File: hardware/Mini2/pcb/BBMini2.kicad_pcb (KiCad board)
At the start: 4 copper layers, 80 x 56 mm, 59 parts, among them J1 Barrel_Jack_Switch, J2 USB_B_Mini, J3 Display, J4 Conn_02x05_Odd_Even, Q1 MBT2222ADW1T1, SW1 SW_SPDT, SW2 SW_Push, SW3 SW_Push, SW4 SW_Push, U1 ESP8266EX, U2 AT25SF081-SSHF-X, U3 AP2112K-3.3, U4 CP2104, U5 MCP3208, Y1 ABM8-26.000MHZ-10-1-U-T

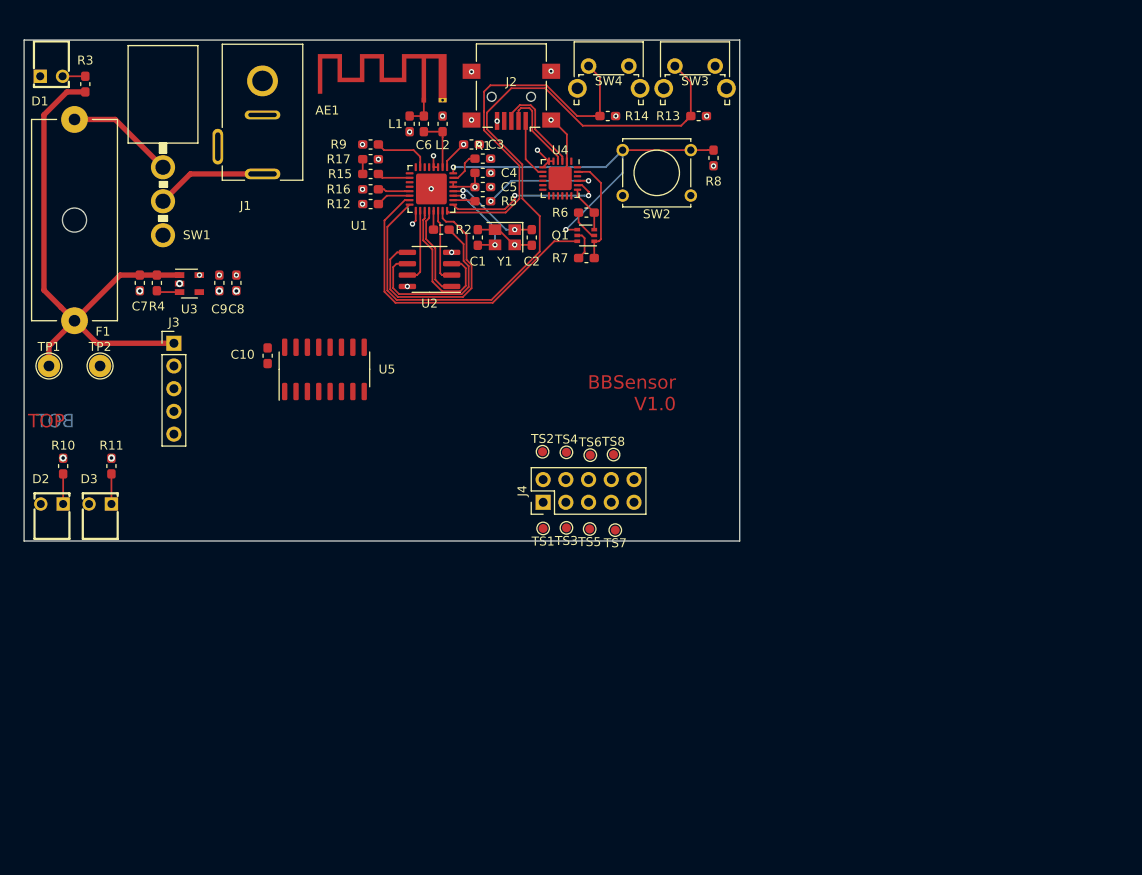
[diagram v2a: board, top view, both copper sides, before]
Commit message: feat: BBMini2 - experimental ESP8266 PCB (SMD)
* add nee stuff

Issue #23
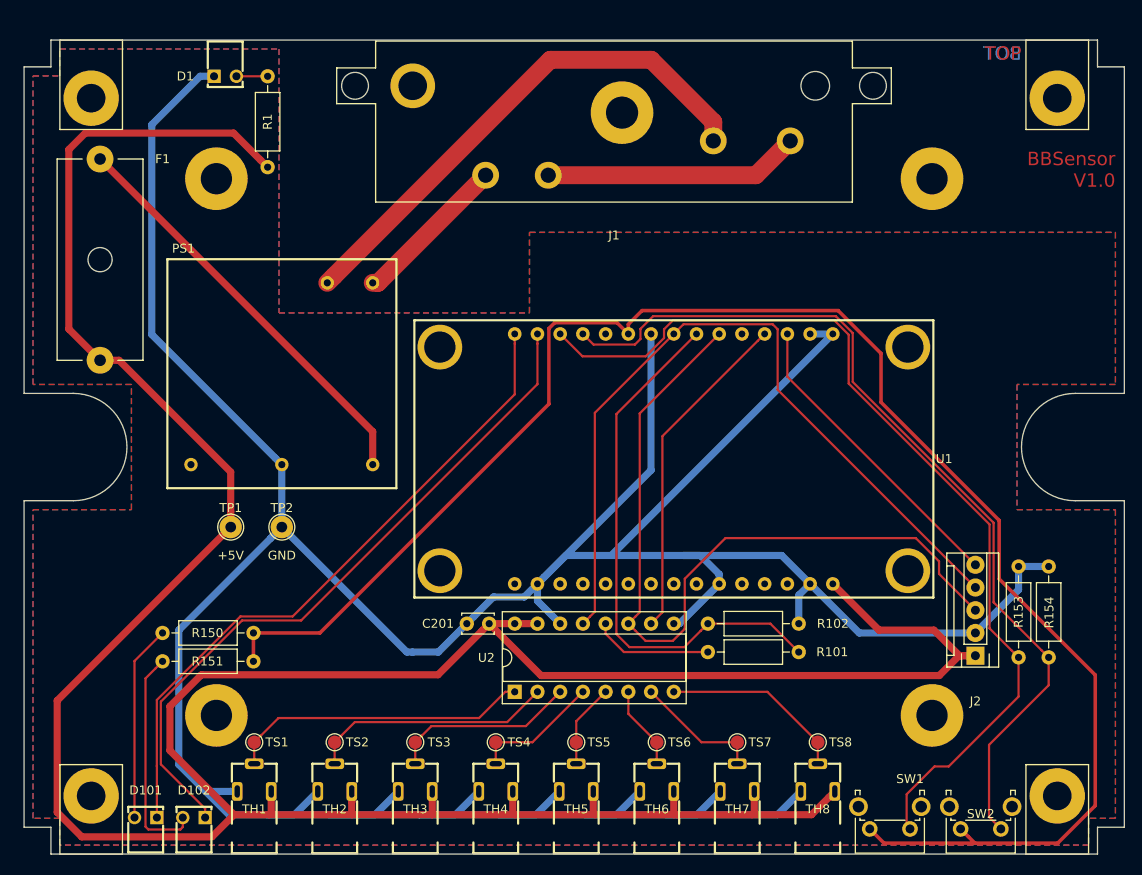
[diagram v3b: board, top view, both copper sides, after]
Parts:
- removed AE1: Antenna_Shield, RF_Antenna:Texas_SWRA117D_2.4GHz_Left
- removed C1, C2: 10p, Capacitor_SMD:C_0603_1608Metric_Pad1.05x0.95mm_HandSolder
- removed C10, C3, C4, C5: 100n, Capacitor_SMD:C_0603_1608Metric_Pad1.05x0.95mm_HandSolder
- removed C6: 5p6, Capacitor_SMD:C_0603_1608Metric_Pad1.05x0.95mm_HandSolder
- removed C7, C8: 10u, Capacitor_SMD:C_0603_1608Metric_Pad1.05x0.95mm_HandSolder
- removed C9: 1u, Capacitor_SMD:C_0603_1608Metric_Pad1.05x0.95mm_HandSolder
- removed D2: LED_RED, VCC:5600F
- removed D3: LED_GREEN, VCC:5600F
- removed J3: Display, Connector_PinHeader_2.54mm:PinHeader_1x05_P2.54mm_Vertical
- removed J4: Conn_02x05_Odd_Even, Connector_PinHeader_2.54mm:PinHeader_2x05_P2.54mm_Vertical
- removed L1, L2: L, Inductor_SMD:L_0603_1608Metric_Pad1.05x0.95mm_HandSolder
- removed Q1: MBT2222ADW1T1, Package_TO_SOT_SMD:SOT-363_SC-70-6
- removed R10, R11: 140, Resistor_SMD:R_0603_1608Metric_Pad1.05x0.95mm_HandSolder
- removed R12, R4, R5, R6, R7, R8, R9: 10k, Resistor_SMD:R_0603_1608Metric_Pad1.05x0.95mm_HandSolder
- removed R13, R14, R17: 2k2, Resistor_SMD:R_0603_1608Metric_Pad1.05x0.95mm_HandSolder
- removed R15: 1k, Resistor_SMD:R_0603_1608Metric_Pad1.05x0.95mm_HandSolder
- removed R16: 4k7, Resistor_SMD:R_0603_1608Metric_Pad1.05x0.95mm_HandSolder
- removed R2: 200, Resistor_SMD:R_0603_1608Metric_Pad1.05x0.95mm_HandSolder
- removed R3: 220, Resistor_SMD:R_0603_1608Metric_Pad1.05x0.95mm_HandSolder
- removed SW3, SW4: SW_Push, Button_Switch_THT:SW_Tactile_SPST_Angled_PTS645Vx83-2LFS
- removed U3: AP2112K-3.3, Package_TO_SOT_SMD:SOT-23-5
- removed U4: CP2104, Package_DFN_QFN:QFN-24-1EP_4x4mm_P0.5mm_EP2.6x2.6mm
- removed U5: MCP3208, Package_SO:SOIC-16_3.9x9.9mm_P1.27mm
- removed Y1: ABM8-26.000MHZ-10-1-U-T, Crystal:Crystal_SMD_Abracon_ABM8G-4Pin_3.2x2.5mm
- added C201: 100n, Capacitor_THT:C_Disc_D3.4mm_W2.1mm_P2.50mm, F.Cu at (67.0, 80.2)
- added D101: RED, VCC:5600F, F.Cu at (28.6, 105.9)
- added D102: GREEN, VCC:5600F, F.Cu at (34.0, 105.9)
- added PS1: TMPS_05, Traco:Traco_TMPS_05, F.Cu at (43.8, 52.3)
- added R101: 1k, Resistor_THT:R_Axial_DIN0207_L6.3mm_D2.5mm_P10.16mm_Horizontal, F.Cu at (91.4, 83.4)
- added R102: 2k2, Resistor_THT:R_Axial_DIN0207_L6.3mm_D2.5mm_P10.16mm_Horizontal, F.Cu at (91.4, 80.2)
- added R150: 140, Resistor_THT:R_Axial_DIN0207_L6.3mm_D2.5mm_P10.16mm_Horizontal, F.Cu at (40.6, 81.3)
- added R151: 140, Resistor_THT:R_Axial_DIN0207_L6.3mm_D2.5mm_P10.16mm_Horizontal, F.Cu at (40.6, 84.5)
- added R153: 2k2, Resistor_THT:R_Axial_DIN0207_L6.3mm_D2.5mm_P10.16mm_Horizontal, F.Cu at (126.2, 84.0)
- added R154: 2k2, Resistor_THT:R_Axial_DIN0207_L6.3mm_D2.5mm_P10.16mm_Horizontal, F.Cu at (129.5, 84.0)
- added TH1: AudioJack3, Lumberg:LUMBERG_1501_05, F.Cu at (40.7, 105.9)
- added TH2: AudioJack3, Lumberg:LUMBERG_1501_05, F.Cu at (49.7, 105.9)
- added TH3: AudioJack3, Lumberg:LUMBERG_1501_05, F.Cu at (58.7, 105.9)
- added TH4: AudioJack3, Lumberg:LUMBERG_1501_05, F.Cu at (67.7, 105.9)
- added TH5: AudioJack3, Lumberg:LUMBERG_1501_05, F.Cu at (76.7, 105.9)
- added TH6: AudioJack3, Lumberg:LUMBERG_1501_05, F.Cu at (85.7, 105.9)
- added TH7: AudioJack3, Lumberg:LUMBERG_1501_05, F.Cu at (94.7, 105.9)
- added TH8: AudioJack3, Lumberg:LUMBERG_1501_05, F.Cu at (103.7, 105.9)
- added ~: Mounting_Bracket_L10_W7_M3, Collection:Mounting_Bracket_L10_W7_M3, F.Cu at (134.0, 15.0)
- added ~: Mounting_Bracket_L10_W7_M3, Collection:Mounting_Bracket_L10_W7_M3, F.Cu at (26.0, 15.0)
- added ~: Mounting_Bracket_L10_W7_M3, Collection:Mounting_Bracket_L10_W7_M3, F.Cu at (127.0, 106.0)
- added ~: Mounting_Bracket_L10_W7_M3, Collection:Mounting_Bracket_L10_W7_M3, F.Cu at (19.0, 106.0)
- added ~: ~, MountingHole:MountingHole_3.5mm_Pad, F.Cu at (36.5, 30.5)
- added ~: ~, MountingHole:MountingHole_3.5mm_Pad, F.Cu at (36.5, 90.5)
- added ~: ~, MountingHole:MountingHole_3.5mm_Pad, F.Cu at (116.5, 30.5)
- added ~: ~, MountingHole:MountingHole_3.5mm_Pad, F.Cu at (116.5, 90.5)
- J1: value Barrel_Jack_Switch -> Schurter_CMF1; footprint Collection:CLIFF_DC_SOCKET_2.5 -> Schurter:CMF1_Offset
- J2: value USB_B_Mini -> Display; footprint Connector_USB:USB_Mini-B_Lumberg_2486_01_Horizontal -> Molex:Molex_KK256_Pin_Header_Straight_1x05
- R1: value 12k -> 220; footprint Resistor_SMD:R_0603_1608Metric_Pad1.05x0.95mm_HandSolder -> Resistor_THT:R_Axial_DIN0207_L6.3mm_D2.5mm_P10.16mm_Horizontal
- SW1: value SW_SPDT -> SW_Push; footprint Collection:MIYAMA_MS-500-B-VT -> Button_Switch_THT:SW_Tactile_SPST_Angled_PTS645Vx83-2LFS
- SW2: footprint Button_Switch_THT:SW_Tactile_Straight_KSL0Axx1LFTR -> Button_Switch_THT:SW_Tactile_SPST_Angled_PTS645Vx83-2LFS
- TS1, TS2, TS3, TS4, TS5, TS6, TS7, TS8: footprint TestPoint:TestPoint_Pad_D1.0mm -> TestPoint:TestPoint_Pad_D1.5mm
- U1: value ESP8266EX -> ESP8266-12E_NodeMCU_Lolin; footprint Package_DFN_QFN:QFN-32-1EP_5x5mm_P0.5mm_EP3.45x3.45mm -> Collection:ESP8266-12E_NodeMCU_Lolin
- U2: value AT25SF081-SSHF-X -> MCP3208; footprint Package_SO:SOIC-8_3.9x4.9mm_P1.27mm -> Package_DIP:DIP-16_W7.62mm_Socket
- moved SW1 110.5 mm to (114.0, 103.2), turned to 180 degrees
- moved J2 81.2 mm to (121.3, 83.8)
- moved SW2 78.8 mm to (124.2, 103.2)
- moved U2 48.2 mm to (69.8, 87.9), turned to 90 degrees
- moved J1 42.0 mm to (80.9, 15.1), turned to 0 degrees
- moved TS1 40.2 mm to (40.7, 93.5)
- moved TS2 39.9 mm to (49.7, 93.5), turned to 180 degrees
- moved TS8 39.4 mm to (103.7, 93.5), turned to 180 degrees
- moved TS4 33.4 mm to (67.7, 93.5), turned to 180 degrees
- moved TS6 32.9 mm to (85.7, 93.5), turned to 180 degrees
- moved U1 31.6 mm to (69.8, 61.8), turned to 90 degrees
- moved TS3 29.3 mm to (58.7, 93.5)
- moved TS7 27.4 mm to (94.7, 93.5)
- moved TP1 27.2 mm to (38.1, 69.4)
- moved TP2 27.2 mm to (43.8, 69.4)
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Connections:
- net /ESP8266EX/ADC renamed Net-(U1-Pad6)
- J1 pad 2: GND -> Net-(J1-Pad2)
- J2 pad 1: Net-(J2-Pad1) -> +5V
- J2 pad 2: Net-(J2-Pad2) -> GND
- J2 pad 3: Net-(J2-Pad3) -> /Analog/Digital/SPI1
- J2 pad 4: Net-(J2-Pad4) -> /Analog/Digital/SPI3
- J2 pad 5: GND -> /Display/SPI5
- R1 pad 1: Net-(R1-Pad1) -> Net-(D1-Pad2)
- R1 pad 2: GND -> +5V
- SW1 pad 1: Net-(SW1-Pad1) -> Net-(R153-Pad1)
- SW1 pad 2: Net-(J1-Pad1) -> +3V3
- SW2 pad 1: GND -> Net-(R154-Pad1)
- SW2 pad 2: /ESP8266EX/~RST -> +3V3
- TS1 pad 1: /Temperature/SIGNAL1 -> /Analog/Digital/SIGNAL1
- TS2 pad 1: /Temperature/SIGNAL2 -> /Analog/Digital/SIGNAL2
- TS3 pad 1: /Temperature/SIGNAL3 -> /Analog/Digital/SIGNAL3
- TS4 pad 1: /Temperature/SIGNAL4 -> /Analog/Digital/SIGNAL4
- TS5 pad 1: /Temperature/SIGNAL5 -> /Analog/Digital/SIGNAL5
- TS6 pad 1: /Temperature/SIGNAL6 -> /Analog/Digital/SIGNAL6
- TS7 pad 1: /Temperature/SIGNAL7 -> /Analog/Digital/SIGNAL7
- TS8 pad 1: /Temperature/SIGNAL8 -> /Analog/Digital/SIGNAL8
- U1 pad 1: +3V3 -> Net-(U1-Pad1)
- U1 pad 10: /ESP8266EX/GPIO12 -> GND
- U1 pad 11: +3V3 -> Net-(U1-Pad11)
- U1 pad 12: /ESP8266EX/GPIO13 -> Net-(U1-Pad12)
- U1 pad 13: /ESP8266EX/GPIO15 -> Net-(U1-Pad13)
- U1 pad 14: /ESP8266EX/GPIO2 -> GND
- U1 pad 15: /ESP8266EX/GPIO0 -> +5V
- U1 pad 16: /ESP8266EX/GPIO4 -> Net-(D101-Pad1)
- U1 pad 17: +3V3 -> Net-(D102-Pad1)
- U1 pad 18: /ESP8266EX/SDIO_DATA_2 -> Net-(R153-Pad1)
- U1 pad 19: /ESP8266EX/SDIO_DATA_3 -> Net-(R154-Pad1)
- U1 pad 2: /ESP8266EX/LNA -> GND
- U1 pad 20: /ESP8266EX/SDIO_CMD -> Net-(U1-Pad20)
- U1 pad 21: /ESP8266EX/SDIO_CLK -> +3V3
- U1 pad 22: /ESP8266EX/SDIO_DATA_0 -> GND
- U1 pad 23: /ESP8266EX/SDIO_DATA_1 -> /Analog/Digital/SPI3
- U1 pad 24: /ESP8266EX/GPIO5 -> /ESP8266/MISO
- U1 pad 25: /ESP8266EX/GPIO1_TXD -> /Analog/Digital/SPI1
- U1 pad 26: /ESP8266EX/GPIO3_RXD -> Net-(U1-Pad26)
- U1 pad 27: /ESP8266EX/XTAL_OUT -> /Analog/Digital/SPI4
- U1 pad 28: /ESP8266EX/XTAL_IN -> /Display/SPI5
- U1 pad 29: +3V3 -> GND
- U1 pad 3: +3V3 -> Net-(U1-Pad3)
- U1 pad 30: +3V3 -> GND
- U1 pad 4: +3V3 -> Net-(U1-Pad4)
- U1 pad 7: /ESP8266EX/EN -> Net-(U1-Pad7)
- U1 pad 8: /IO/CS1 -> Net-(U1-Pad8)
- U1 pad 9: /ESP8266EX/GPIO14 -> Net-(U1-Pad9)
- U2 pad 1: /ESP8266EX/SDIO_CMD -> /Analog/Digital/SIGNAL1
- U2 pad 2: /ESP8266EX/SDIO_DATA_0 -> /Analog/Digital/SIGNAL2
- U2 pad 3: /ESP8266EX/SDIO_DATA_3 -> /Analog/Digital/SIGNAL3
- U2 pad 4: GND -> /Analog/Digital/SIGNAL4
- U2 pad 5: /ESP8266EX/SDIO_DATA_1 -> /Analog/Digital/SIGNAL5
- U2 pad 6: Net-(R2-Pad1) -> /Analog/Digital/SIGNAL6
- U2 pad 7: /ESP8266EX/SDIO_DATA_2 -> /Analog/Digital/SIGNAL7
- U2 pad 8: +3V3 -> /Analog/Digital/SIGNAL8
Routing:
- net GND: track 14.4 -> 411.9 mm, vias 22 -> 0
- net +5V: track 62.4 -> 361.1 mm
- net +3V3: track 14.5 -> 187.2 mm, vias 14 -> 0
- net Net-(R153-Pad1): track 0.00 -> 105.6 mm
- net Net-(R154-Pad1): track 0.00 -> 101.2 mm
- net /Analog/Digital/SPI1: track 0.00 -> 88.4 mm
- net /Analog/Digital/SPI3: track 0.00 -> 86.9 mm
- net /ESP8266EX/GPIO4: track 80.8 -> 0.00 mm
- net Net-(D102-Pad1): track 0.00 -> 77.4 mm
- net Net-(D101-Pad1): track 0.00 -> 74.1 mm
- net /ESP8266/MISO: track 0.00 -> 60.7 mm
- net Net-(J1-Pad1): track 12.4 -> 58.5 mm
- net /ESP8266EX/~RST: track 43.4 -> 0.00 mm, vias 2 -> 0
- net /ESP8266EX/GPIO5: track 43.2 -> 0.00 mm
- net /Analog/Digital/SPI4: track 0.00 -> 37.6 mm
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- added copper zone on F.Cu, net +5V
- added copper zone on B.Cu, net GND
- removed copper zone on In1.Cu, net +3V3
- removed copper zone on In2.Cu, net GND
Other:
- board size 80 x 56 mm -> 123 x 91 mm
- copper layers 4 -> 2
- net class 3V3: clearance 0.125 -> 0.3; trace_width 0.2 -> 0.4; via_dia 0.6 -> 0.8; via_drill 0.3 -> 0.4
- net class 5V: clearance 0.2 -> 0.3; trace_width 0.6 -> 0.8
- net class AC added: clearance 0.4, trace_width 2, via_dia 0.8, via_drill 0.4
- net class Default: clearance 0.125 -> 0.2; trace_width 0.2 -> 0.25; via_dia 0.6 -> 0.8; via_drill 0.3 -> 0.4
- rule trace_clearance: 0.125 -> 0.2
- board text added: "+5V"
- board text added: "GND"

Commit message: feat: BBMini2 - experimental ESP8266 PCB (SMD)
* add reference_

Issue #23
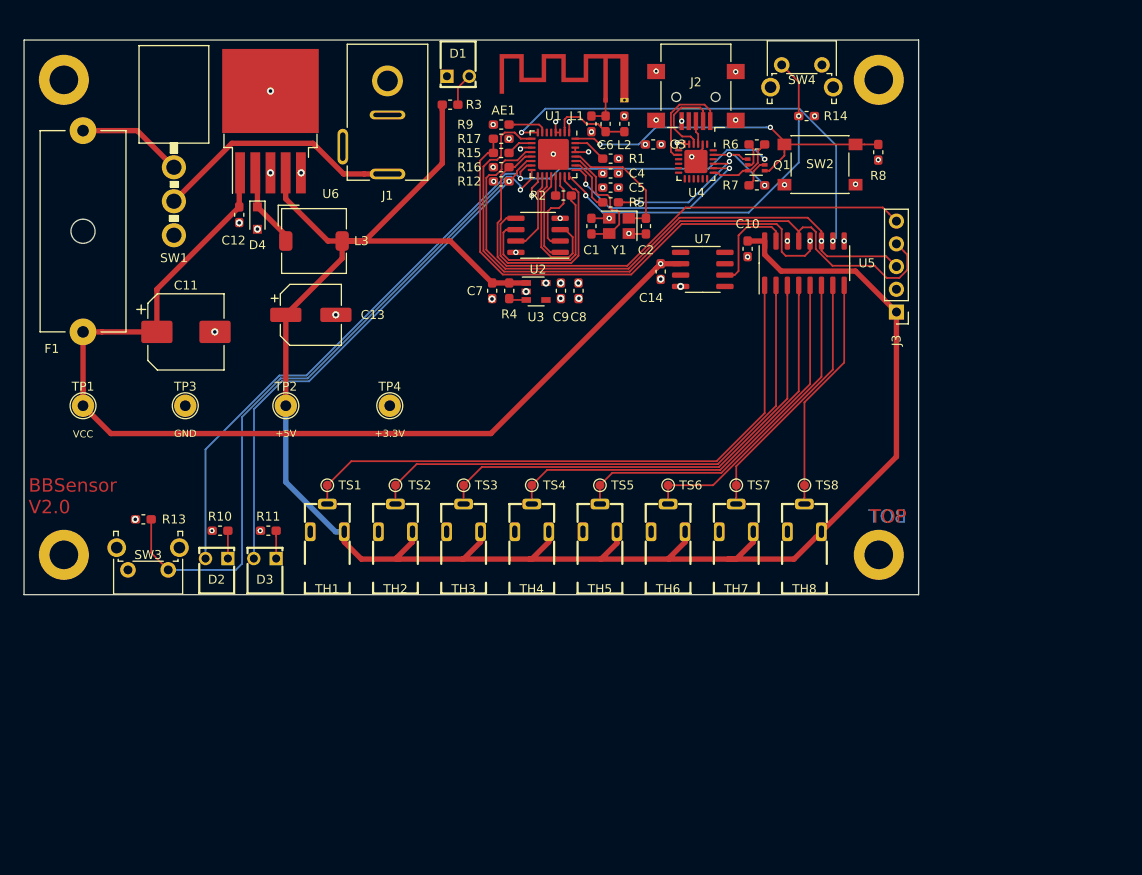
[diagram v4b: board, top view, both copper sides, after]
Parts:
- removed C201: 100n, Capacitor_THT:C_Disc_D3.4mm_W2.1mm_P2.50mm
- removed D101: RED, VCC:5600F
- removed D102: GREEN, VCC:5600F
- removed PS1: TMPS_05, Traco:Traco_TMPS_05
- removed R101: 1k, Resistor_THT:R_Axial_DIN0207_L6.3mm_D2.5mm_P10.16mm_Horizontal
- removed R102, R153, R154: 2k2, Resistor_THT:R_Axial_DIN0207_L6.3mm_D2.5mm_P10.16mm_Horizontal
- removed R150, R151: 140, Resistor_THT:R_Axial_DIN0207_L6.3mm_D2.5mm_P10.16mm_Horizontal
- removed the ~ at (134.0, 15.0)
- removed the ~ at (26.0, 15.0)
- removed the ~ at (127.0, 106.0)
- removed the ~ at (19.0, 106.0)
- removed the ~ at (36.5, 30.5)
- removed the ~ at (36.5, 90.5)
- removed the ~ at (116.5, 30.5)
- removed the ~ at (116.5, 90.5)
- added AE1: Antenna_Shield, RF_Antenna:Texas_SWRA117D_2.4GHz_Left, F.Cu at (80.0, 21.7)
- added C1: 10p, Capacitor_SMD:C_0603_1608Metric_Pad1.05x0.95mm_HandSolder, F.Cu at (78.4, 35.8)
- added C10: 100n, Capacitor_SMD:C_0603_1608Metric_Pad1.05x0.95mm_HandSolder, F.Cu at (95.9, 38.3)
- added C11: 100u, Capacitor_SMD:CP_Elec_8x10, F.Cu at (33.1, 47.6)
- added C12: 100n, Capacitor_SMD:C_0603_1608Metric_Pad1.05x0.95mm_HandSolder, F.Cu at (39.1, 34.5)
- added C13: 100u, Capacitor_SMD:CP_Elec_6.3x5.9, F.Cu at (47.1, 45.7)
- added C14: 100n, Capacitor_SMD:C_0603_1608Metric_Pad1.05x0.95mm_HandSolder, F.Cu at (86.2, 40.9)
- added C2: 10p, Capacitor_SMD:C_0603_1608Metric_Pad1.05x0.95mm_HandSolder, F.Cu at (84.5, 35.8)
- added C3: 100n, Capacitor_SMD:C_0603_1608Metric_Pad1.05x0.95mm_HandSolder, F.Cu at (85.3, 26.7)
- added C4: 100n, Capacitor_SMD:C_0603_1608Metric_Pad1.05x0.95mm_HandSolder, F.Cu at (80.6, 29.9)
- added C5: 100n, Capacitor_SMD:C_0603_1608Metric_Pad1.05x0.95mm_HandSolder, F.Cu at (80.6, 31.5)
- added C6: 5p6, Capacitor_SMD:C_0603_1608Metric_Pad1.05x0.95mm_HandSolder, F.Cu at (80.0, 24.4)
- added C7: 10u, Capacitor_SMD:C_0603_1608Metric_Pad1.05x0.95mm_HandSolder, F.Cu at (67.3, 43.0)
- added C8: 10u, Capacitor_SMD:C_0603_1608Metric_Pad1.05x0.95mm_HandSolder, F.Cu at (77.0, 43.0)
- added C9: 1u, Capacitor_SMD:C_0603_1608Metric_Pad1.05x0.95mm_HandSolder, F.Cu at (75.0, 43.0)
- added D2: LED_RED, VCC:5600F, F.Cu at (36.5, 77.0)
- added D3: LED_GREEN, VCC:5600F, F.Cu at (41.9, 77.0)
- added D4: 1N5822, Diode_SMD:D_SOD-323_HandSoldering, F.Cu at (41.1, 34.9)
- added J3: Display, Connector_PinHeader_2.54mm:PinHeader_1x05_P2.54mm_Vertical, F.Cu at (112.5, 45.4)
- added L1: L, Inductor_SMD:L_0603_1608Metric_Pad1.05x0.95mm_HandSolder, F.Cu at (78.4, 24.4)
- added L2: L, Inductor_SMD:L_0603_1608Metric_Pad1.05x0.95mm_HandSolder, F.Cu at (82.1, 24.4)
- added L3: 100u, Inductor_SMD:L_TDK_SLF7032, F.Cu at (47.4, 37.5)
- added Q1: MBT2222ADW1T1, Package_TO_SOT_SMD:SOT-363_SC-70-6, F.Cu at (96.8, 29.0)
- added R10: 140, Resistor_SMD:R_0603_1608Metric_Pad1.05x0.95mm_HandSolder, F.Cu at (36.9, 69.8)
- added R11: 140, Resistor_SMD:R_0603_1608Metric_Pad1.05x0.95mm_HandSolder, F.Cu at (42.3, 69.8)
- added R12: 10k, Resistor_SMD:R_0603_1608Metric_Pad1.05x0.95mm_HandSolder, F.Cu at (68.3, 30.8)
- added R13: 2k2, Resistor_SMD:R_0603_1608Metric_Pad1.05x0.95mm_HandSolder, F.Cu at (28.3, 68.6)
- added R14: 2k2, Resistor_SMD:R_0603_1608Metric_Pad1.05x0.95mm_HandSolder, F.Cu at (102.5, 23.5)
- added R15: 1k, Resistor_SMD:R_0603_1608Metric_Pad1.05x0.95mm_HandSolder, F.Cu at (68.3, 27.6)
- added R16: 4k7, Resistor_SMD:R_0603_1608Metric_Pad1.05x0.95mm_HandSolder, F.Cu at (68.3, 29.2)
- added R17: 2k2, Resistor_SMD:R_0603_1608Metric_Pad1.05x0.95mm_HandSolder, F.Cu at (68.3, 26.0)
- added R2: 200, Resistor_SMD:R_0603_1608Metric_Pad1.05x0.95mm_HandSolder, F.Cu at (75.3, 32.4)
- added R3: 220, Resistor_SMD:R_0603_1608Metric_Pad1.05x0.95mm_HandSolder, F.Cu at (62.6, 22.2)
- added R4: 10k, Resistor_SMD:R_0603_1608Metric_Pad1.05x0.95mm_HandSolder, F.Cu at (69.2, 43.0)
- added R5: 10k, Resistor_SMD:R_0603_1608Metric_Pad1.05x0.95mm_HandSolder, F.Cu at (80.6, 33.1)
- added R6: 10k, Resistor_SMD:R_0603_1608Metric_Pad1.05x0.95mm_HandSolder, F.Cu at (96.9, 26.7)
- added R7: 10k, Resistor_SMD:R_0603_1608Metric_Pad1.05x0.95mm_HandSolder, F.Cu at (96.9, 31.2)
- added R8: 10k, Resistor_SMD:R_0603_1608Metric_Pad1.05x0.95mm_HandSolder, F.Cu at (110.5, 27.5)
- added R9: 10k, Resistor_SMD:R_0603_1608Metric_Pad1.05x0.95mm_HandSolder, F.Cu at (68.3, 24.4)
- added SW3: SW_Push, Button_Switch_THT:SW_Tactile_SPST_Angled_PTS645Vx83-2LFS, F.Cu at (31.1, 74.2)
- added SW4: SW_Push, Button_Switch_THT:SW_Tactile_SPST_Angled_PTS645Vx83-2LFS, F.Cu at (99.7, 17.8)
- added TP3: TestPoint, TestPoint:TestPoint_THTPad_D2.5mm_Drill1.2mm, F.Cu at (33.0, 55.9)
- added TP4: TestPoint, TestPoint:TestPoint_THTPad_D2.5mm_Drill1.2mm, F.Cu at (55.9, 55.9)
- added U3: AP2112K-3.3, Package_TO_SOT_SMD:SOT-23-5, F.Cu at (72.2, 43.1)
- added U4: CP2104, Package_DFN_QFN:QFN-24-1EP_4x4mm_P0.5mm_EP2.6x2.6mm, F.Cu at (90.1, 28.6)
- added U5: MCP3208, Package_SO:SOIC-16_3.9x9.9mm_P1.27mm, F.Cu at (102.2, 39.9)
- added U6: LM2576S-5, Package_TO_SOT_SMD:TO-263-5_TabPin3, F.Cu at (42.5, 24.1)
- added U7: REF02AU, Package_SO:SOIC-8_3.9x4.9mm_P1.27mm, F.Cu at (90.9, 40.6)
- added Y1: ABM8-26.000MHZ-10-1-U-T, Crystal:Crystal_SMD_Abracon_ABM8G-4Pin_3.2x2.5mm, F.Cu at (81.5, 35.8)
- added ~: MountingHole_3.2mm_M3_DIN965_Pad, MountingHole:MountingHole_3.2mm_M3_DIN965_Pad, F.Cu at (110.5, 19.4)
- added ~: MountingHole_3.2mm_M3_DIN965_Pad, MountingHole:MountingHole_3.2mm_M3_DIN965_Pad, F.Cu at (110.5, 72.5)
- added ~: MountingHole_3.2mm_M3_DIN965_Pad, MountingHole:MountingHole_3.2mm_M3_DIN965_Pad, F.Cu at (19.4, 72.5)
- added ~: MountingHole_3.2mm_M3_DIN965_Pad, MountingHole:MountingHole_3.2mm_M3_DIN965_Pad, F.Cu at (19.4, 19.4)
- J1: value Schurter_CMF1 -> Barrel_Jack_Switch; footprint Schurter:CMF1_Offset -> Collection:CLIFF_DC_SOCKET_2.5
- J2: value Display -> USB_B_Mini; footprint Molex:Molex_KK256_Pin_Header_Straight_1x05 -> Connector_USB:USB_Mini-B_Lumberg_2486_01_Horizontal
- R1: value 220 -> 12k; footprint Resistor_THT:R_Axial_DIN0207_L6.3mm_D2.5mm_P10.16mm_Horizontal -> Resistor_SMD:R_0603_1608Metric_Pad1.05x0.95mm_HandSolder
- SW1: value SW_Push -> SW_SPDT; footprint Button_Switch_THT:SW_Tactile_SPST_Angled_PTS645Vx83-2LFS -> Collection:MIYAMA_MS-500-B-VT
- SW2: footprint Button_Switch_THT:SW_Tactile_SPST_Angled_PTS645Vx83-2LFS -> Button_Switch_SMD:SW_Push_1P1T_NO_6x6mm_H9.5mm
- TS1, TS2, TS3, TS4, TS5, TS6, TS7, TS8: footprint TestPoint:TestPoint_Pad_D1.5mm -> TestPoint:TestPoint_Pad_D1.0mm
- U1: value ESP8266-12E_NodeMCU_Lolin -> ESP8266EX; footprint Collection:ESP8266-12E_NodeMCU_Lolin -> Package_DFN_QFN:QFN-32-1EP_5x5mm_P0.5mm_EP3.45x3.45mm
- U2: value MCP3208 -> AT25SF081-SSHF-X; footprint Package_DIP:DIP-16_W7.62mm_Socket -> Package_SO:SOIC-8_3.9x4.9mm_P1.27mm
- moved SW1 109.6 mm to (35.6, 26.5), turned to 90 degrees
- moved SW2 77.0 mm to (104.0, 28.9)
- moved J2 69.8 mm to (90.1, 21.4)
- moved U2 51.1 mm to (72.5, 36.8), turned to 180 degrees
- moved R1 39.4 mm to (80.6, 28.3), turned to 0 degrees
- moved U1 34.3 mm to (74.2, 27.8), turned to 270 degrees
- moved TH1 30.2 mm to (48.9, 76.9)
- moved TS1 29.9 mm to (48.9, 64.8)
- moved TH2 29.8 mm to (56.5, 76.9)
- moved TH3 29.5 mm to (64.1, 76.9)
- moved TS2 29.5 mm to (56.5, 64.8), turned to 0 degrees
- moved J1 29.4 mm to (55.6, 30.0), turned to 270 degrees
- moved TH4 29.3 mm to (71.8, 76.9)
- moved TS3 29.2 mm to (64.1, 64.8), turned to 0 degrees
- moved TH5 29.2 mm to (79.4, 76.9)
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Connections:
- net Net-(U1-Pad6) renamed /ESP8266EX/ADC
- F1 pad 1: +5V -> VCC
- J1 pad 2: Net-(J1-Pad2) -> GND
- J2 pad 1: +5V -> Net-(J2-Pad1)
- J2 pad 2: GND -> Net-(J2-Pad2)
- J2 pad 3: /Analog/Digital/SPI1 -> Net-(J2-Pad3)
- J2 pad 4: /Analog/Digital/SPI3 -> Net-(J2-Pad4)
- J2 pad 5: /Display/SPI5 -> GND
- R1 pad 1: Net-(D1-Pad2) -> Net-(R1-Pad1)
- R1 pad 2: +5V -> GND
- SW1 pad 1: Net-(R153-Pad1) -> Net-(SW1-Pad1)
- SW1 pad 2: +3V3 -> Net-(J1-Pad1)
- SW2 pad 1: Net-(R154-Pad1) -> GND
- SW2 pad 2: +3V3 -> /ESP8266EX/~RST
- TH1 pad T: /Analog/Digital/SIGNAL1 -> /Temperature/SIGNAL1
- TH2 pad T: /Analog/Digital/SIGNAL2 -> /Temperature/SIGNAL2
- TH3 pad T: /Analog/Digital/SIGNAL3 -> /Temperature/SIGNAL3
- TH4 pad T: /Analog/Digital/SIGNAL4 -> /Temperature/SIGNAL4
- TH5 pad T: /Analog/Digital/SIGNAL5 -> /Temperature/SIGNAL5
- TH6 pad T: /Analog/Digital/SIGNAL6 -> /Temperature/SIGNAL6
- TH7 pad T: /Analog/Digital/SIGNAL7 -> /Temperature/SIGNAL7
- TH8 pad T: /Analog/Digital/SIGNAL8 -> /Temperature/SIGNAL8
- TP1 pad 1: +5V -> VCC
- TP2 pad 1: GND -> +5V
- TS1 pad 1: /Analog/Digital/SIGNAL1 -> /Temperature/SIGNAL1
- TS2 pad 1: /Analog/Digital/SIGNAL2 -> /Temperature/SIGNAL2
- TS3 pad 1: /Analog/Digital/SIGNAL3 -> /Temperature/SIGNAL3
- TS4 pad 1: /Analog/Digital/SIGNAL4 -> /Temperature/SIGNAL4
- TS5 pad 1: /Analog/Digital/SIGNAL5 -> /Temperature/SIGNAL5
- TS6 pad 1: /Analog/Digital/SIGNAL6 -> /Temperature/SIGNAL6
- TS7 pad 1: /Analog/Digital/SIGNAL7 -> /Temperature/SIGNAL7
- TS8 pad 1: /Analog/Digital/SIGNAL8 -> /Temperature/SIGNAL8
- U1 pad 1: Net-(U1-Pad1) -> +3V3
- U1 pad 10: GND -> /ESP8266EX/GPIO12
- U1 pad 11: Net-(U1-Pad11) -> +3V3
- U1 pad 12: Net-(U1-Pad12) -> /ESP8266EX/GPIO13
- U1 pad 13: Net-(U1-Pad13) -> /ESP8266EX/GPIO15
- U1 pad 14: GND -> /ESP8266EX/GPIO2
- U1 pad 15: +5V -> /ESP8266EX/GPIO0
- U1 pad 16: Net-(D101-Pad1) -> /ESP8266EX/GPIO4
- U1 pad 17: Net-(D102-Pad1) -> +3V3
- U1 pad 18: Net-(R153-Pad1) -> /ESP8266EX/SDIO_DATA_2
- U1 pad 19: Net-(R154-Pad1) -> /ESP8266EX/SDIO_DATA_3
- U1 pad 2: GND -> /ESP8266EX/LNA
- U1 pad 20: Net-(U1-Pad20) -> /ESP8266EX/SDIO_CMD
- U1 pad 21: +3V3 -> /ESP8266EX/SDIO_CLK
- U1 pad 22: GND -> /ESP8266EX/SDIO_DATA_0
- U1 pad 23: /Analog/Digital/SPI3 -> /ESP8266EX/SDIO_DATA_1
- U1 pad 24: /ESP8266/MISO -> /ESP8266EX/GPIO5
- U1 pad 25: /Analog/Digital/SPI1 -> /ESP8266EX/GPIO1_TXD
- U1 pad 26: Net-(U1-Pad26) -> /ESP8266EX/GPIO3_RXD
- U1 pad 27: /Analog/Digital/SPI4 -> /ESP8266EX/XTAL_OUT
- U1 pad 28: /Display/SPI5 -> /ESP8266EX/XTAL_IN
- U1 pad 29: GND -> +3V3
- U1 pad 3: Net-(U1-Pad3) -> +3V3
- U1 pad 30: GND -> +3V3
- U1 pad 4: Net-(U1-Pad4) -> +3V3
- U1 pad 7: Net-(U1-Pad7) -> /ESP8266EX/EN
- U1 pad 8: Net-(U1-Pad8) -> /IO/CS1
- U1 pad 9: Net-(U1-Pad9) -> /ESP8266EX/GPIO14
- U2 pad 1: /Analog/Digital/SIGNAL1 -> /ESP8266EX/SDIO_CMD
- U2 pad 2: /Analog/Digital/SIGNAL2 -> /ESP8266EX/SDIO_DATA_0
- U2 pad 3: /Analog/Digital/SIGNAL3 -> /ESP8266EX/SDIO_DATA_3
- U2 pad 4: /Analog/Digital/SIGNAL4 -> GND
- U2 pad 5: /Analog/Digital/SIGNAL5 -> /ESP8266EX/SDIO_DATA_1
- U2 pad 6: /Analog/Digital/SIGNAL6 -> Net-(R2-Pad1)
- U2 pad 7: /Analog/Digital/SIGNAL7 -> /ESP8266EX/SDIO_DATA_2
- U2 pad 8: /Analog/Digital/SIGNAL8 -> +3V3
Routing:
- net GND: track 411.9 -> 6.02 mm, vias 0 -> 38
- net +3V3: track 187.2 -> 11.0 mm, vias 0 -> 18
- net +5V: track 361.1 -> 223.4 mm
- net VCC: track 0.00 -> 114.1 mm, vias 0 -> 1
- net Net-(R153-Pad1): track 105.6 -> 0.00 mm
- net Net-(R154-Pad1): track 101.2 -> 0.00 mm
- net /ESP8266EX/GPIO0: track 0.00 -> 91.9 mm, vias 0 -> 2
- net /Analog/Digital/SPI1: track 88.4 -> 0.00 mm
- net /Analog/Digital/SPI3: track 86.9 -> 0.00 mm
- net /ESP8266EX/GPIO14: track 0.00 -> 78.7 mm
- net Net-(D102-Pad1): track 77.4 -> 0.00 mm
- net /ESP8266EX/GPIO4: track 0.00 -> 77.4 mm, vias 0 -> 1
- net Net-(D101-Pad1): track 74.1 -> 0.00 mm
- net /Temperature/SIGNAL1: track 0.00 -> 68.6 mm
- net /ESP8266EX/GPIO13: track 0.00 -> 67.3 mm, vias 0 -> 1
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- added copper zone on In1.Cu, net +3V3
- added copper zone on In2.Cu, net GND
- removed copper zone on F.Cu, net +5V
- removed copper zone on B.Cu, net GND
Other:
- board size 123 x 91 mm -> 100 x 62 mm
- copper layers 2 -> 4
- net class 3V3: clearance 0.3 -> 0.125; trace_width 0.4 -> 0.2; via_dia 0.8 -> 0.6; via_drill 0.4 -> 0.3
- net class 5V: clearance 0.3 -> 0.2; trace_width 0.8 -> 0.6
- net class AC removed
- net class Default: clearance 0.2 -> 0.125; trace_width 0.25 -> 0.2; via_dia 0.8 -> 0.6; via_drill 0.4 -> 0.3
- rule trace_clearance: 0.2 -> 0.125
- board text added: "+3.3V"
- board text added: "BBSensor V2.0"
- board text added: "VCC"
- board text removed: "BBSensor V1.0"

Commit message: feat: BBMini2 - experimental ESP8266 PCB (SMD)
* redo Mini2

Issue #23
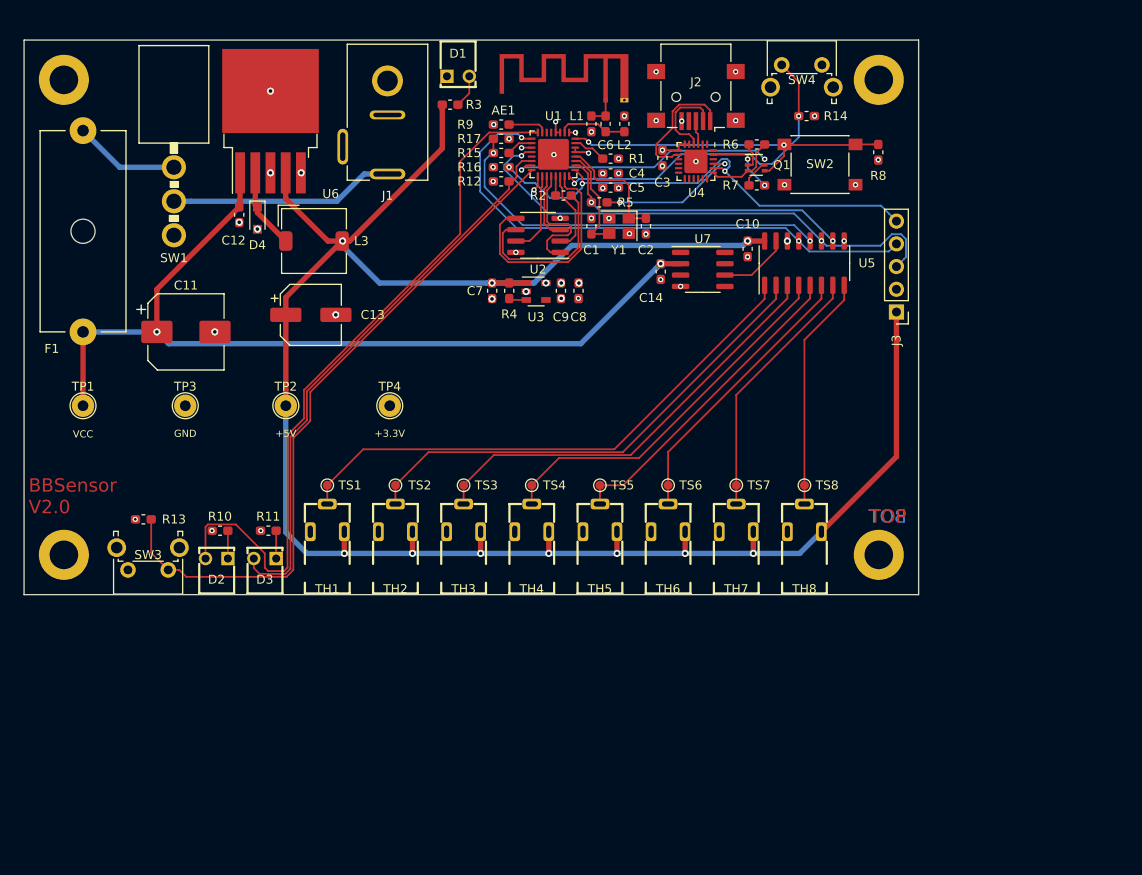
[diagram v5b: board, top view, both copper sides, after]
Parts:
- moved C3 1.83 mm to (86.4, 28.2), turned to 270 degrees
- moved R5 1.27 mm to (79.3, 33.1)
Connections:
- D2 pad 2: /ESP8266EX/GPIO0 -> /ESP8266EX/GPIO16
- J3 pad 5: /ESP8266EX/GPIO15 -> /ESP8266EX/GPIO1_TXD
- R16 pad 1: /ESP8266EX/GPIO15 -> /ESP8266EX/GPIO1_TXD
- R5 pad 2: /ESP8266EX/GPIO3_RXD -> /IO/CS1
- U1 pad 13: /ESP8266EX/GPIO15 -> Net-(U1-Pad13)
- U1 pad 26: /ESP8266EX/GPIO3_RXD -> /IO/CS1
- U1 pad 8: /IO/CS1 -> /ESP8266EX/GPIO16
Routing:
- net /ESP8266EX/GPIO16: track 0.00 -> 79.5 mm
- net /ESP8266EX/GPIO0: track 91.9 -> 29.8 mm
- net /ESP8266EX/GPIO15: track 61.9 -> 0.00 mm
- net /ESP8266EX/GPIO1_TXD: track 23.2 -> 54.3 mm, vias 2 -> 3
- net /ESP8266EX/GPIO14: track 78.7 -> 60.9 mm, vias 0 -> 2
- net /IO/CS1: track 50.6 -> 34.0 mm
- net /IO/MISO: track 58.2 -> 44.8 mm, vias 1 -> 2
- net VCC: track 114.1 -> 100.9 mm, vias 1 -> 2
- net /ESP8266EX/GPIO13: track 67.3 -> 56.9 mm, vias 1 -> 2
- net /ESP8266EX/SDIO_DATA_3: track 15.9 -> 7.46 mm
- net /Temperature/SIGNAL1: track 68.6 -> 61.1 mm
- net /Temperature/SIGNAL2: track 61.8 -> 54.8 mm
- net /Temperature/SIGNAL3: track 55.0 -> 48.4 mm
- net /Temperature/SIGNAL4: track 48.1 -> 42.1 mm
- net /ESP8266EX/GPIO3_RXD: track 6.08 -> 0.00 mm
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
